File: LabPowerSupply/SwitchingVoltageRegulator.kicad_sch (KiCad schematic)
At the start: 16 parts

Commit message: Rev 1.0 done
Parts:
- added C5_SVR2: (no value), symbol Device:C
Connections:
- net 3.3 Volt: now also C5_SVR2.1
- net GND: now also C5_SVR2.2
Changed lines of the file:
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@@
   (junction (at 158.75 119.38) (diameter 0) (color 0 0 0 0)
   )
+  (junction (at 86.36 105.41) (diameter 0) (color 0 0 0 0)
+  )
+  (junction (at 97.79 97.79) (diameter 0) (color 0 0 0 0)
+  )
   (junction (at 86.36 87.63) (diameter 0) (color 0 0 0 0)
   )
@@
   (junction (at 138.43 100.33) (diameter 0) (color 0 0 0 0)
   )
-  (junction (at 86.36 104.14) (diameter 0) (color 0 0 0 0)
-  )
   (junction (at 166.37 97.79) (diameter 0) (color 0 0 0 0)
   )
   (junction (at 166.37 92.71) (diameter 0) (color 0 0 0 0)
   )
+  (junction (at 97.79 105.41) (diameter 0) (color 0 0 0 0)
+  )
   (junction (at 140.97 92.71) (diameter 0) (color 0 0 0 0)
   )
@@
     (stroke (width 0) (type default) (color 0 0 0 0))
   )
+  (wire (pts (xy 85.09 105.41) (xy 86.36 105.41))
+    (stroke (width 0) (type default) (color 0 0 0 0))
+  )
   (wire (pts (xy 140.97 76.2) (xy 171.45 76.2))
     (stroke (width 0) (type default) (color 0 0 0 0))
@@
     (stroke (width 0) (type default) (color 0 0 0 0))
   )
+  (wire (pts (xy 96.52 97.79) (xy 97.79 97.79))
+    (stroke (width 0) (type default) (color 0 0 0 0))
+  )
   (wire (pts (xy 110.49 127) (xy 118.11 127))
     (stroke (width 0) (type default) (color 0 0 0 0))
@@
     (stroke (width 0) (type default) (color 0 0 0 0))
   )
-  (wire (pts (xy 85.09 104.14) (xy 86.36 104.14))
+  (wire (pts (xy 97.79 97.79) (xy 110.49 97.79))
     (stroke (width 0) (type default) (color 0 0 0 0))
   )
@@
     (stroke (width 0) (type default) (color 0 0 0 0))
   )
-  (wire (pts (xy 118.11 104.14) (xy 118.11 119.38))
+  (wire (pts (xy 118.11 105.41) (xy 118.11 119.38))
     (stroke (width 0) (type default) (color 0 0 0 0))
   )
@@
     (stroke (width 0) (type default) (color 0 0 0 0))
   )
-  (wire (pts (xy 86.36 95.25) (xy 86.36 104.14))
+  (wire (pts (xy 86.36 95.25) (xy 86.36 105.41))
     (stroke (width 0) (type default) (color 0 0 0 0))
   )
@@
     (stroke (width 0) (type default) (color 0 0 0 0))
   )
-  (wire (pts (xy 86.36 104.14) (xy 118.11 104.14))
+  (wire (pts (xy 86.36 105.41) (xy 97.79 105.41))
     (stroke (width 0) (type default) (color 0 0 0 0))
   )
@@
   )
   (wire (pts (xy 118.11 127) (xy 118.11 134.62))
+    (stroke (width 0) (type default) (color 0 0 0 0))
+  )
+  (wire (pts (xy 97.79 105.41) (xy 118.11 105.41))
     (stroke (width 0) (type default) (color 0 0 0 0))
   )
@@
     (effects (font (size 1.27 1.27)) (justify left))
   )
-  (hierarchical_label "GND" (shape input) (at 85.09 104.14 180)
+  (hierarchical_label "GND" (shape input) (at 85.09 105.41 180)
     (effects (font (size 1.27 1.27)) (justify right))
   )
@@
     (effects (font (size 1.27 1.27)) (justify right))
   )
-  (hierarchical_label "3.3 Volt" (shape output) (at 110.49 97.79 180)
+  (hierarchical_label "3.3 Volt" (shape output) (at 96.52 97.79 180)
     (effects (font (size 1.27 1.27)) (justify right))
   )
@@
       (effects (font (size 1.27 1.27)) hide)
     )
+    (pin "1")
+    (pin "2")
+  )
+  (symbol (lib_id "Device:C") (at 97.79 101.6 0) (unit 1)
+    (in_bom yes) (on_board yes)
+    (property "Reference" "C5_SVR2" (id 0) (at 101.6 100.3299 0)
+      (effects (font (size 1.27 1.27)) (justify left))
+    )
+    (property "Value" "" (id 1) (at 101.6 102.8699 0)
+      (effects (font (size 1.27 1.27)) (justify left))
+    )
+    (property "Footprint" "" (id 2) (at 98.7552 105.41 0)
+      (effects (font (size 1.27 1.27)) hide)
+    )
+    (property "Datasheet" "~" (id 3) (at 97.79 101.6 0)
+      (effects (font (size 1.27 1.27)) hide)
+    )

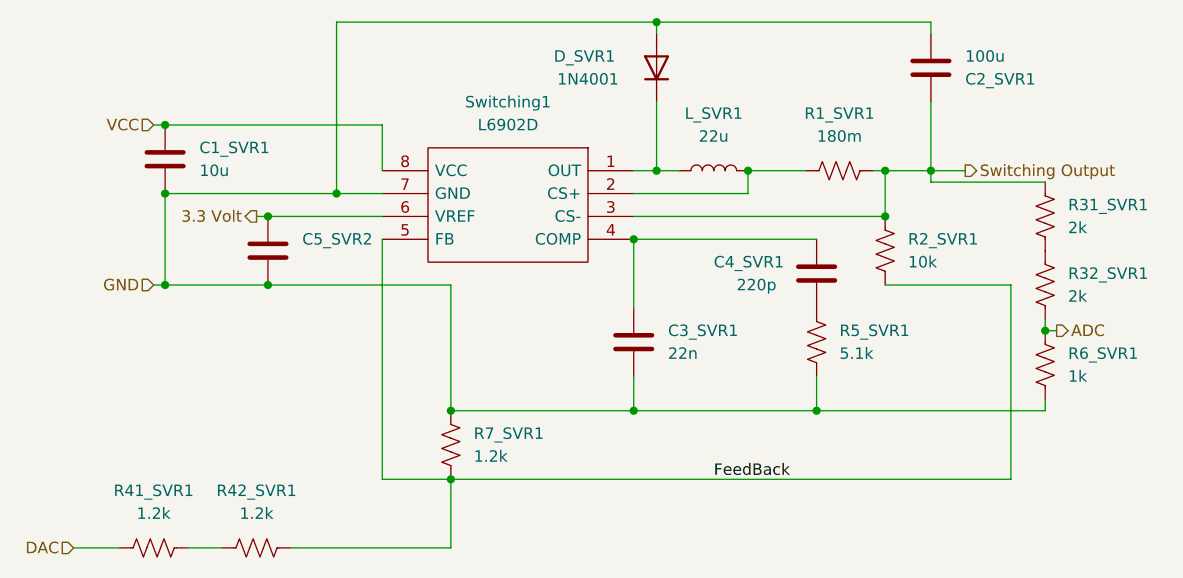
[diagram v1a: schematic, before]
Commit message: Updated Part List
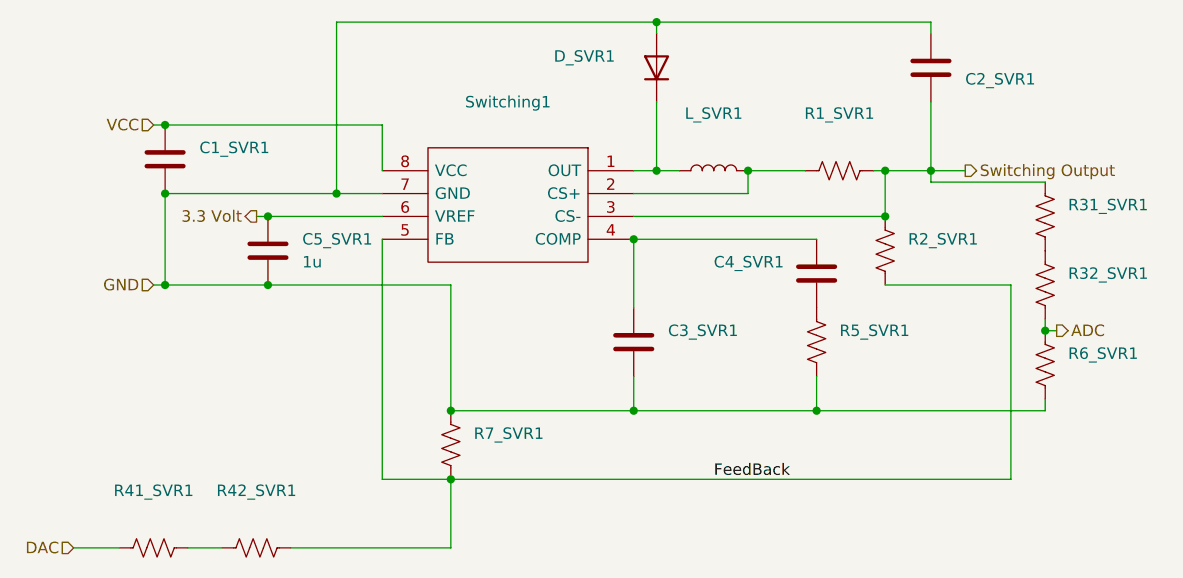
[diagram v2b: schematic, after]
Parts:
- C1_SVR1: value 10u -> (none); footprint Capacitor_SMD:C_1206_3216Metric -> (none)
- C2_SVR1: value 100u -> (none); footprint Capacitor_THT:C_Radial_D8.0mm_H7.0mm_P3.50mm -> (none)
- C3_SVR1: value 22n -> (none); footprint Capacitor_SMD:C_0603_1608Metric -> (none)
- C4_SVR1: value 220p -> (none); footprint Capacitor_SMD:C_0603_1608Metric -> (none)
- C5_SVR1: renamed from C5_SVR2; value (none) -> 1u
- D_SVR1: value 1N4001 -> (none); footprint Diode_SMD:D_SMA -> (none)
- L_SVR1: value 22u -> (none); footprint Inductor_SMD:L_Sumida_CR75 -> (none)
- R1_SVR1: value 180m -> (none); footprint Resistor_SMD:R_0603_1608Metric -> (none)
- R2_SVR1: value 10k -> (none); footprint Resistor_SMD:R_0603_1608Metric -> (none)
- R31_SVR1, R32_SVR1: value 2k -> (none); footprint Resistor_SMD:R_0603_1608Metric -> (none)
- R41_SVR1, R42_SVR1, R7_SVR1: value 1.2k -> (none); footprint Resistor_SMD:R_0603_1608Metric -> (none)
- R5_SVR1: value 5.1k -> (none); footprint Resistor_SMD:R_0603_1608Metric -> (none)
- R6_SVR1: value 1k -> (none); footprint Resistor_SMD:R_0603_1608Metric -> (none)
- Switching1: value L6902D -> (none); footprint Package_SO:SO-8_3.9x4.9mm_P1.27mm -> (none)
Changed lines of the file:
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@@
       (effects (font (size 1.27 1.27)) (justify left))
     )
-    (property "Value" "1.2k" (id 1) (at 120.65 124.4599 0)
-      (effects (font (size 1.27 1.27)) (justify left))
-    )
-    (property "Footprint" "Resistor_SMD:R_0603_1608Metric" (id 2) (at 119.126 123.444 90)
+    (property "Value" "" (id 1) (at 120.65 124.4599 0)
+      (effects (font (size 1.27 1.27)) (justify left))
+    )
+    (property "Footprint" "" (id 2) (at 119.126 123.444 90)
       (effects (font (size 1.27 1.27)) hide)
     )
@@
     (in_bom yes) (on_board yes) (fields_autoplaced)
     (property "Reference" "R1_SVR1" (id 0) (at 161.29 86.36 90))
-    (property "Value" "180m" (id 1) (at 161.29 88.9 90))
-    (property "Footprint" "Resistor_SMD:R_0603_1608Metric" (id 2) (at 161.544 91.694 90)
+    (property "Value" "" (id 1) (at 161.29 88.9 90))
+    (property "Footprint" "" (id 2) (at 161.544 91.694 90)
       (effects (font (size 1.27 1.27)) hide)
     )
@@
       (effects (font (size 1.27 1.27)) (justify right))
     )
-    (property "Value" "1N4001" (id 1) (at 133.35 82.55 90))
-    (property "Footprint" "Diode_SMD:D_SMA" (id 2) (at 145.415 81.28 0)
+    (property "Value" "" (id 1) (at 133.35 82.55 90))
+    (property "Footprint" "" (id 2) (at 145.415 81.28 0)
       (effects (font (size 1.27 1.27)) hide)
     )
@@
       (effects (font (size 1.27 1.27)) (justify left))
     )
-    (property "Value" "22n" (id 1) (at 142.24 113.0299 0)
-      (effects (font (size 1.27 1.27)) (justify left))
-    )
-    (property "Footprint" "Capacitor_SMD:C_0603_1608Metric" (id 2) (at 139.3952 115.57 0)
+    (property "Value" "" (id 1) (at 142.24 113.0299 0)
+      (effects (font (size 1.27 1.27)) (justify left))
+    )
+    (property "Footprint" "" (id 2) (at 139.3952 115.57 0)
       (effects (font (size 1.27 1.27)) hide)
     )
@@
     (in_bom yes) (on_board yes) (fields_autoplaced)
     (property "Reference" "Switching1" (id 0) (at 124.46 85.09 0))
-    (property "Value" "L6902D" (id 1) (at 124.46 87.63 0))
-    (property "Footprint" "Package_SO:SO-8_3.9x4.9mm_P1.27mm" (id 2) (at 114.3 90.17 0)
+    (property "Value" "" (id 1) (at 124.46 87.63 0))
+    (property "Footprint" "" (id 2) (at 114.3 90.17 0)
       (effects (font (size 1.27 1.27)) (justify left) hide)
     )
@@
     (in_bom yes) (on_board yes) (fields_autoplaced)
     (property "Reference" "L_SVR1" (id 0) (at 147.32 86.36 90))
-    (property "Value" "22u" (id 1) (at 147.32 88.9 90))
-    (property "Footprint" "Inductor_SMD:L_Sumida_CR75" (id 2) (at 147.32 92.71 0)
+    (property "Value" "" (id 1) (at 147.32 88.9 90))
+    (property "Footprint" "" (id 2) (at 147.32 92.71 0)
       (effects (font (size 1.27 1.27)) hide)
     )
@@
       (effects (font (size 1.27 1.27)) (justify left))
     )
-    (property "Value" "2k" (id 1) (at 186.69 99.0599 0)
-      (effects (font (size 1.27 1.27)) (justify left))
-    )
-    (property "Footprint" "Resistor_SMD:R_0603_1608Metric" (id 2) (at 185.166 98.044 90)
+    (property "Value" "" (id 1) (at 186.69 99.0599 0)
+      (effects (font (size 1.27 1.27)) (justify left))
+    )
+    (property "Footprint" "" (id 2) (at 185.166 98.044 90)
       (effects (font (size 1.27 1.27)) hide)
     )
@@
     (in_bom yes) (on_board yes) (fields_autoplaced)
     (property "Reference" "R41_SVR1" (id 0) (at 85.09 128.27 90))
-    (property "Value" "1.2k" (id 1) (at 85.09 130.81 90))
-    (property "Footprint" "Resistor_SMD:R_0603_1608Metric" (id 2) (at 84.836 135.636 90)
+    (property "Value" "" (id 1) (at 85.09 130.81 90))
+    (property "Footprint" "" (id 2) (at 84.836 135.636 90)
       (effects (font (size 1.27 1.27)) hide)
     )
@@
       (effects (font (size 1.27 1.27)) (justify left))
     )
-    (property "Value" "1k" (id 1) (at 186.69 115.5699 0)
-      (effects (font (size 1.27 1.27)) (justify left))
-    )
-    (property "Footprint" "Resistor_SMD:R_0603_1608Metric" (id 2) (at 185.166 114.554 90)
+    (property "Value" "" (id 1) (at 186.69 115.5699 0)
+      (effects (font (size 1.27 1.27)) (justify left))
+    )
+    (property "Footprint" "" (id 2) (at 185.166 114.554 90)
       (effects (font (size 1.27 1.27)) hide)
     )
@@
     (in_bom yes) (on_board yes) (fields_autoplaced)
     (property "Reference" "R42_SVR1" (id 0) (at 96.52 128.27 90))
-    (property "Value" "1.2k" (id 1) (at 96.52 130.81 90))
-    (property "Footprint" "Resistor_SMD:R_0603_1608Metric" (id 2) (at 96.266 135.636 90)
+    (property "Value" "" (id 1) (at 96.52 130.81 90))
+    (property "Footprint" "" (id 2) (at 96.266 135.636 90)
       (effects (font (size 1.27 1.27)) hide)
     )
@@
       (effects (font (size 1.27 1.27)) (justify left))
     )
-    (property "Value" "10u" (id 1) (at 90.17 92.7099 0)
-      (effects (font (size 1.27 1.27)) (justify left))
-    )
-    (property "Footprint" "Capacitor_SMD:C_1206_3216Metric" (id 2) (at 87.3252 95.25 0)
+    (property "Value" "" (id 1) (at 90.17 92.7099 0)
+      (effects (font (size 1.27 1.27)) (justify left))
+    )
+    (property "Footprint" "" (id 2) (at 87.3252 95.25 0)
       (effects (font (size 1.27 1.27)) hide)
     )
@@
       (effects (font (size 1.27 1.27)) (justify left))
     )
-    (property "Value" "100u" (id 1) (at 175.26 80.0101 0)
-      (effects (font (size 1.27 1.27)) (justify left))
-    )
-    (property "Footprint" "Capacitor_THT:C_Radial_D8.0mm_H7.0mm_P3.50mm" (id 2) (at 172.4152 77.47 0)
+    (property "Value" "" (id 1) (at 175.26 80.0101 0)
+      (effects (font (size 1.27 1.27)) (justify left))
+    )
+    (property "Footprint" "" (id 2) (at 172.4152 77.47 0)
       (effects (font (size 1.27 1.27)) hide)
     )
@@
       (effects (font (size 1.27 1.27)) (justify left))
     )
-    (property "Value" "220p" (id 1) (at 149.86 105.41 0)
-      (effects (font (size 1.27 1.27)) (justify left))
-    )
-    (property "Footprint" "Capacitor_SMD:C_0603_1608Metric" (id 2) (at 159.7152 107.95 0)
+    (property "Value" "" (id 1) (at 149.86 105.41 0)
+      (effects (font (size 1.27 1.27)) (justify left))
+    )
+    (property "Footprint" "" (id 2) (at 159.7152 107.95 0)
       (effects (font (size 1.27 1.27)) hide)
     )
@@
       (effects (font (size 1.27 1.27)) (justify left))
     )
-    (property "Value" "10k" (id 1) (at 168.91 102.8699 0)
-      (effects (font (size 1.27 1.27)) (justify left))
-    )
-    (property "Footprint" "Resistor_SMD:R_0603_1608Metric" (id 2) (at 167.386 101.854 90)
+    (property "Value" "" (id 1) (at 168.91 102.8699 0)
+      (effects (font (size 1.27 1.27)) (justify left))
+    )
+    (property "Footprint" "" (id 2) (at 167.386 101.854 90)
       (effects (font (size 1.27 1.27)) hide)
     )
@@
   (symbol (lib_id "Device:C") (at 97.79 101.6 0) (unit 1)
     (in_bom yes) (on_board yes)
-    (property "Reference" "C5_SVR2" (id 0) (at 101.6 100.3299 0)
-      (effects (font (size 1.27 1.27)) (justify left))
-    )
-    (property "Value" "" (id 1) (at 101.6 102.8699 0)
+    (property "Reference" "C5_SVR1" (id 0) (at 101.6 100.3299 0)
+      (effects (font (size 1.27 1.27)) (justify left))
+    )
+    (property "Value" "1u" (id 1) (at 101.6 102.8699 0)
       (effects (font (size 1.27 1.27)) (justify left))
     )
@@
       (effects (font (size 1.27 1.27)) (justify left))
     )
-    (property "Value" "5.1k" (id 1) (at 161.29 113.0299 0)
-      (effects (font (size 1.27 1.27)) (justify left))
-    )
-    (property "Footprint" "Resistor_SMD:R_0603_1608Metric" (id 2) (at 159.766 112.014 90)
+    (property "Value" "" (id 1) (at 161.29 113.0299 0)
+      (effects (font (size 1.27 1.27)) (justify left))
+    )
+    (property "Footprint" "" (id 2) (at 159.766 112.014 90)
       (effects (font (size 1.27 1.27)) hide)
     )
@@
       (effects (font (size 1.27 1.27)) (justify left))
     )
-    (property "Value" "2k" (id 1) (at 186.69 106.6799 0)
-      (effects (font (size 1.27 1.27)) (justify left))
-    )
-    (property "Footprint" "Resistor_SMD:R_0603_1608Metric" (id 2) (at 185.166 105.664 90)
-      (effects (font (size 1.27 1.27)) hide)
-    )
+    (property "Value" "" (id 1) (at 186.69 106.6799 0)
+      (effects (font (size 1.27 1.27)) (justify left))
+    )
+    (property "Footprint" "" (id 2) (at 185.166 105.664 90)
+      (effects (font (size 1.27 1.27)) hide)
+    )
